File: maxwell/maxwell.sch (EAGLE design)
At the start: 4 parts

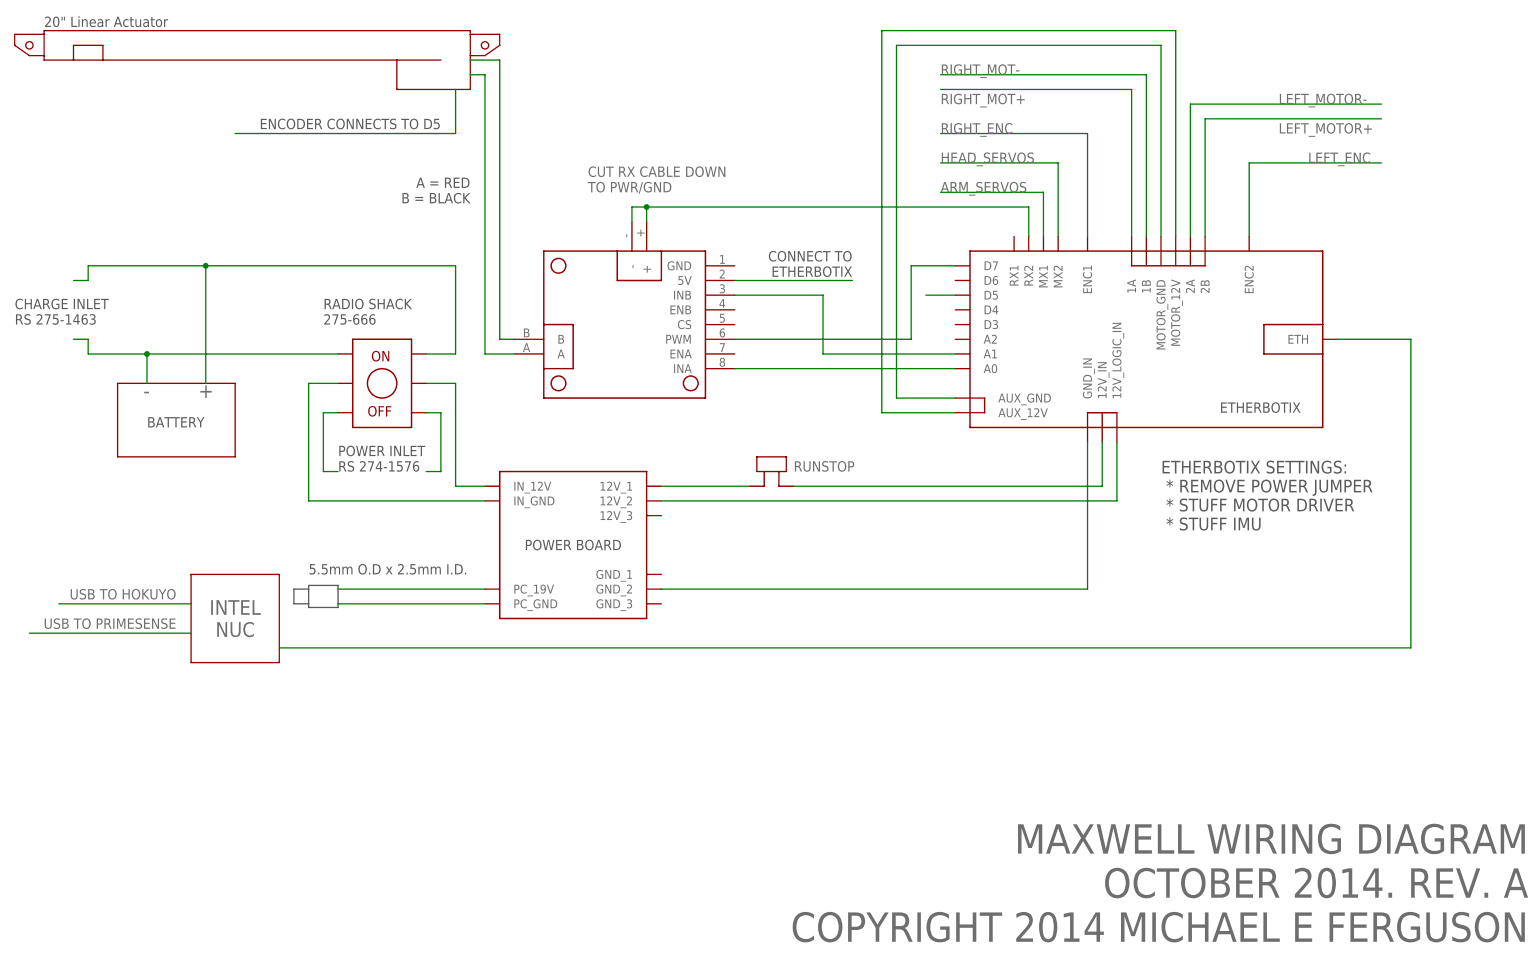
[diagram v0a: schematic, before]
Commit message: fix motor wires that were reversed
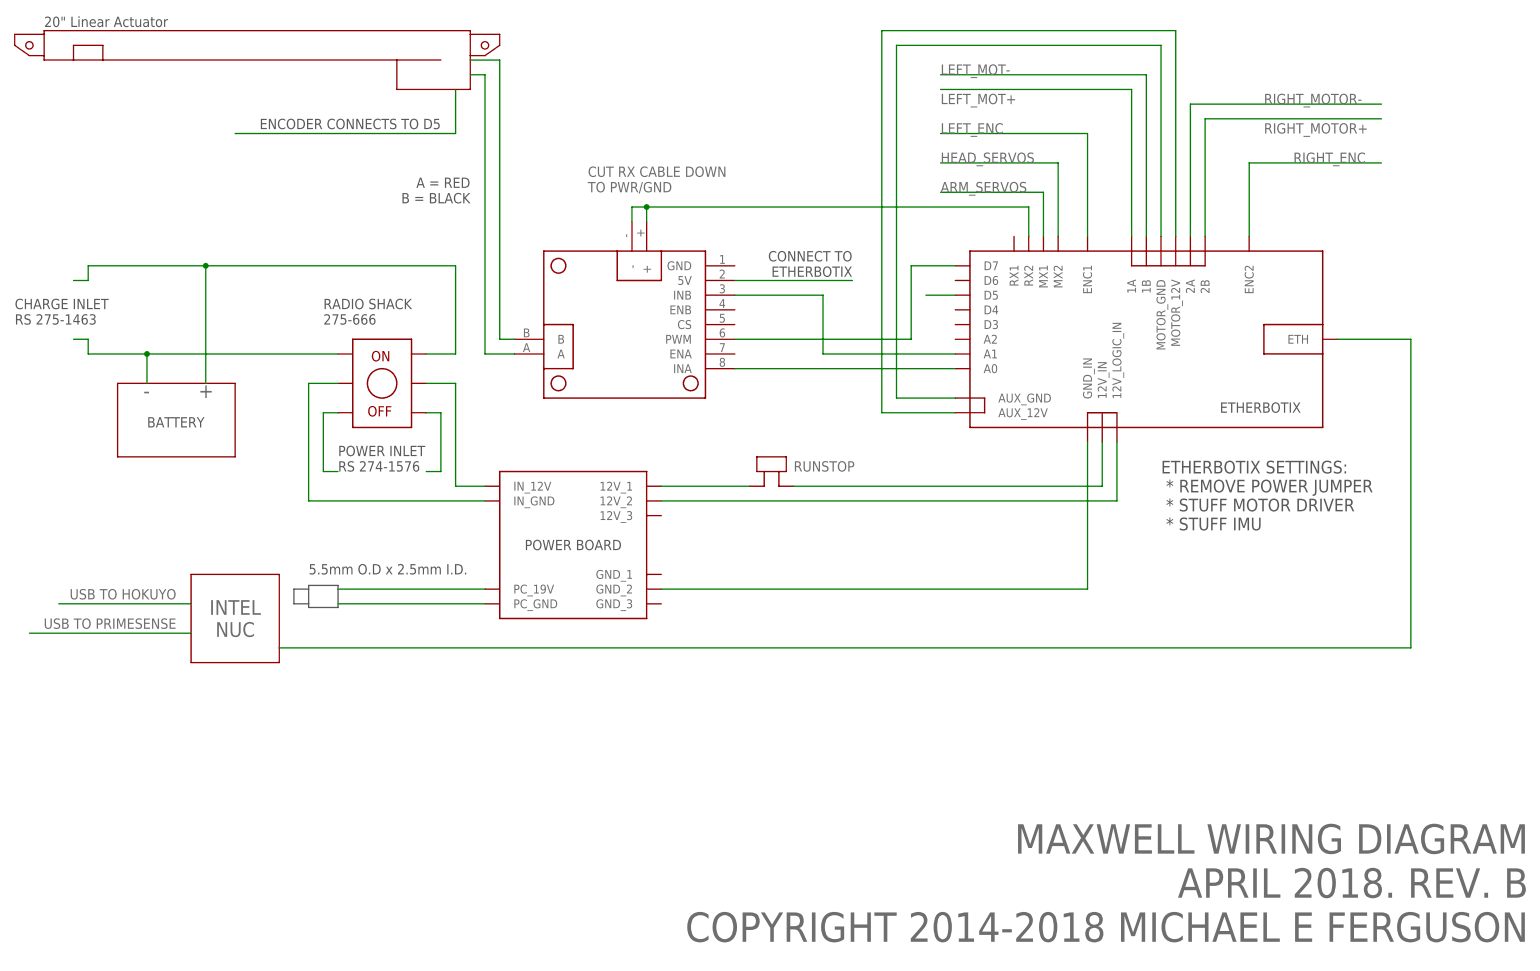
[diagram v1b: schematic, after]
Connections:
- net LEFT_MOTOR+ renamed RIGHT_MOTOR+
- net LEFT_MOTOR- renamed RIGHT_MOTOR-
- net RIGHT_MOT+ renamed LEFT_MOT+
- net RIGHT_MOT- renamed LEFT_MOT-
- net LEFT_ENC: now also U$1.ENC1; no longer U$1.ENC2
- net RIGHT_ENC: now also U$1.ENC2; no longer U$1.ENC1
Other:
- note added: "MAXWELL WIRING DIAGRAM APRIL 2018. REV. B COPYRIGHT 2014-2018 MICHAEL E FERGUSON"
- note removed: "MAXWELL WIRING DIAGRAM OCTOBER 2014. REV. A COPYRIGHT 2014 MICHAEL E FERGUSON"
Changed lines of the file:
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@@
 <text x="147.32" y="83.82" size="1.778" layer="95">RUNSTOP</text>
 <text x="274.32" y="2.54" size="5.08" layer="95" align="bottom-right">MAXWELL WIRING DIAGRAM
-OCTOBER 2014. REV. A
-COPYRIGHT 2014 MICHAEL E FERGUSON</text>
+APRIL 2018. REV. B
+COPYRIGHT 2014-2018 MICHAEL E FERGUSON</text>
 <text x="44.45" y="96.52" size="2.54" layer="95">+</text>
 <text x="34.925" y="96.52" size="2.54" layer="95">-</text>
@@
 </segment>
 </net>
-<net name="LEFT_ENC" class="0">
+<net name="RIGHT_ENC" class="0">
 <segment>
 <pinref part="U$1" gate="G$1" pin="ENC2"/>
 <wire x1="226.06" y1="124.46" x2="226.06" y2="137.16" width="0.1524" layer="91"/>
 <wire x1="226.06" y1="137.16" x2="248.92" y2="137.16" width="0.1524" layer="91"/>
-<label x="236.22" y="137.16" size="1.778" layer="95"/>
+<label x="233.68" y="137.16" size="1.778" layer="95"/>
 </segment>
 </net>
-<net name="RIGHT_ENC" class="0">
+<net name="LEFT_ENC" class="0">
 <segment>
 <pinref part="U$1" gate="G$1" pin="ENC1"/>
@@
 </segment>
 </net>
-<net name="RIGHT_MOT+" class="0">
+<net name="LEFT_MOT+" class="0">
 <segment>
 <pinref part="U$1" gate="G$1" pin="1A"/>
@@
 </segment>
 </net>
-<net name="LEFT_MOTOR+" class="0">
+<net name="RIGHT_MOTOR+" class="0">
 <segment>
 <pinref part="U$1" gate="G$1" pin="2B"/>
 <wire x1="218.44" y1="124.46" x2="218.44" y2="144.78" width="0.1524" layer="91"/>
 <wire x1="218.44" y1="144.78" x2="248.92" y2="144.78" width="0.1524" layer="91"/>
-<label x="231.14" y="142.24" size="1.778" layer="95"/>
+<label x="228.6" y="142.24" size="1.778" layer="95"/>
 </segment>
 </net>
-<net name="LEFT_MOTOR-" class="0">
+<net name="RIGHT_MOTOR-" class="0">
 <segment>
 <pinref part="U$1" gate="G$1" pin="2A"/>
 <wire x1="215.9" y1="124.46" x2="215.9" y2="147.32" width="0.1524" layer="91"/>
 <wire x1="215.9" y1="147.32" x2="248.92" y2="147.32" width="0.1524" layer="91"/>
-<label x="231.14" y="147.32" size="1.778" layer="95"/>
+<label x="228.6" y="147.32" size="1.778" layer="95"/>
 </segment>
 </net>
-<net name="RIGHT_MOT-" class="0">
+<net name="LEFT_MOT-" class="0">
 <segment>
 <pinref part="U$1" gate="G$1" pin="1B"/>
